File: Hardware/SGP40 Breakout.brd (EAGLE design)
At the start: 25.4 x 25.4 mm, 44 parts, among them J2 QWIIC_RIGHT_ANGLE, J4 QWIIC_RIGHT_ANGLE, U1 SGP40

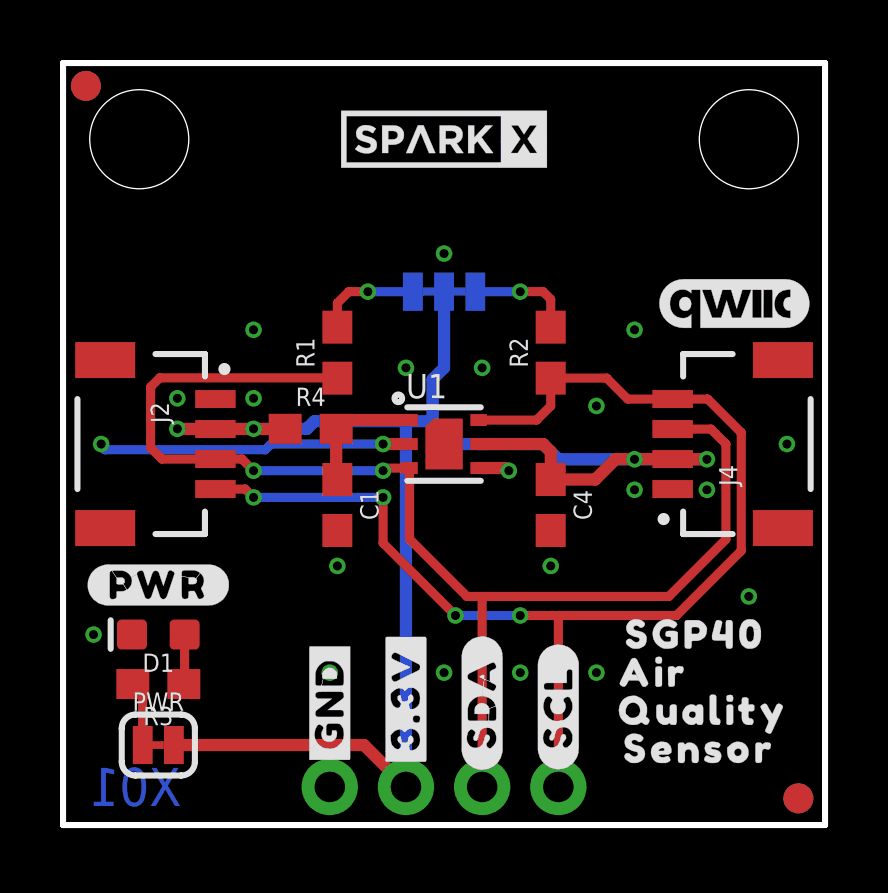
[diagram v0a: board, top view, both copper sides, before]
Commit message: Update logos on board
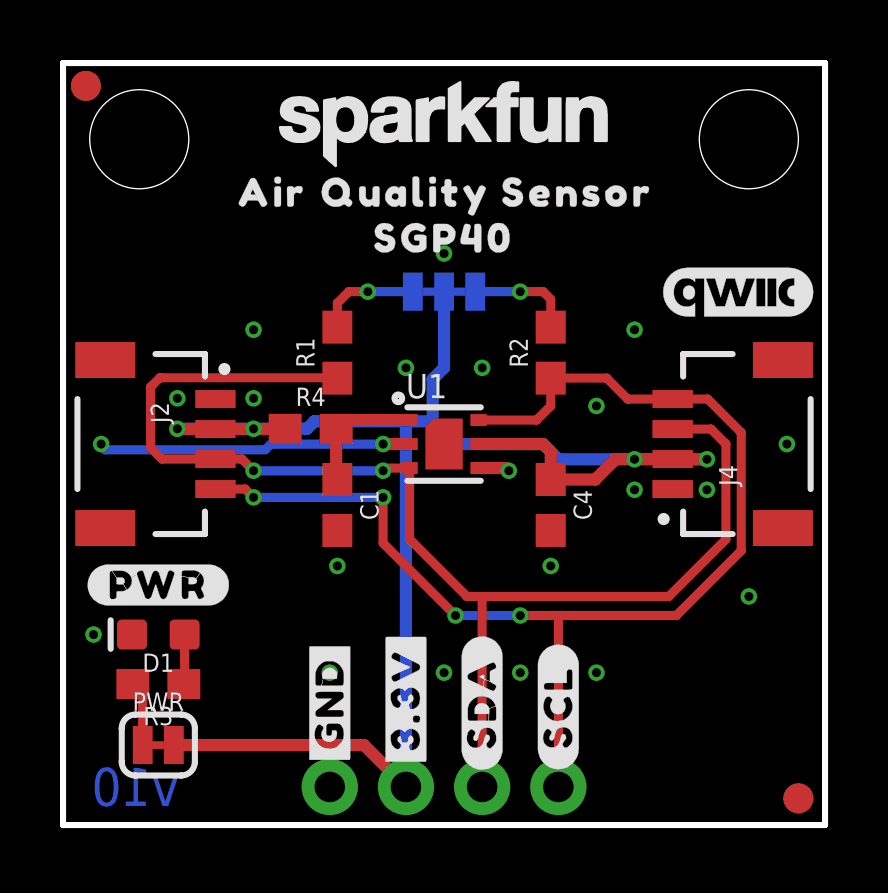
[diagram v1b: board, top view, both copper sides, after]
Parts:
- removed U$10, U$18: SPARKX-LOGO3, SparkX:SPARKX-SMALL
- removed U$16: (no value), SparkFun-Aesthetics:QWIIC_5MM
- added LOGO2: QWIIC_LOGO_5MM, SparkFun-Aesthetics:QWIIC_5MM
- added LOGO3, LOGO6: SFE_LOGO_NAME.1_INCH, SparkFun-Aesthetics:SFE_LOGO_NAME_.1
- added LOGO4: SFE_LOGO_FLAME.1_INCH, SparkFun-Aesthetics:SFE_LOGO_FLAME_.1
- moved U$23 20.4 mm to (6.99, 21.1)
- moved U$25 19.9 mm to (11.4, 21.1)
- moved U$29 19.0 mm to (17.1, 21.1)
- moved U$19 15.6 mm to (12.7, 19.6)
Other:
- board text added: "Revised by: Priyanka Makin"
- board text added: "v10"
- board text removed: "X01"
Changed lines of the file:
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@@
 <?xml version="1.0" encoding="utf-8"?>
 <!DOCTYPE eagle SYSTEM "eagle.dtd">
-<eagle version="9.6.2">
+<eagle version="9.5.2">
 <drawing>
 <settings>
@@
 <layer number="23" name="tOrigins" color="15" fill="1" visible="yes" active="yes"/>
 <layer number="24" name="bOrigins" color="15" fill="1" visible="yes" active="yes"/>
-<layer number="25" name="tNames" color="7" fill="1" visible="yes" active="yes"/>
-<layer number="26" name="bNames" color="7" fill="1" visible="yes" active="yes"/>
-<layer number="27" name="tValues" color="7" fill="1" visible="yes" active="yes"/>
-<layer number="28" name="bValues" color="7" fill="1" visible="yes" active="yes"/>
-<layer number="29" name="tStop" color="7" fill="3" visible="yes" active="yes"/>
-<layer number="30" name="bStop" color="7" fill="6" visible="yes" active="yes"/>
-<layer number="31" name="tCream" color="7" fill="4" visible="yes" active="yes"/>
-<layer number="32" name="bCream" color="7" fill="5" visible="yes" active="yes"/>
-<layer number="33" name="tFinish" color="6" fill="3" visible="yes" active="yes"/>
-<layer number="34" name="bFinish" color="6" fill="6" visible="yes" active="yes"/>
-<layer number="35" name="tGlue" color="7" fill="4" visible="yes" active="yes"/>
-<layer number="36" name="bGlue" color="7" fill="5" visible="yes" active="yes"/>
-<layer number="37" name="tTest" color="7" fill="1" visible="yes" active="yes"/>
-<layer number="38" name="bTest" color="7" fill="1" visible="yes" active="yes"/>
-<layer number="39" name="tKeepout" color="4" fill="11" visible="yes" active="yes"/>
-<layer number="40" name="bKeepout" color="1" fill="11" visible="yes" active="yes"/>
-<layer number="41" name="tRestrict" color="4" fill="10" visible="yes" active="yes"/>
-<layer number="42" name="bRestrict" color="1" fill="10" visible="yes" active="yes"/>
-<layer number="43" name="vRestrict" color="2" fill="10" visible="yes" active="yes"/>
-<layer number="44" name="Drills" color="7" fill="1" visible="yes" active="yes"/>
+<layer number="25" name="tNames" color="7" fill="1" visible="no" active="yes"/>
+<layer number="26" name="bNames" color="7" fill="1" visible="no" active="yes"/>
+<layer number="27" name="tValues" color="7" fill="1" visible="no" active="yes"/>
+<layer number="28" name="bValues" color="7" fill="1" visible="no" active="yes"/>
+<layer number="29" name="tStop" color="7" fill="3" visible="no" active="yes"/>
+<layer number="30" name="bStop" color="7" fill="6" visible="no" active="yes"/>
+<layer number="31" name="tCream" color="7" fill="4" visible="no" active="yes"/>
+<layer number="32" name="bCream" color="7" fill="5" visible="no" active="yes"/>
+<layer number="33" name="tFinish" color="6" fill="3" visible="no" active="yes"/>
+<layer number="34" name="bFinish" color="6" fill="6" visible="no" active="yes"/>
+<layer number="35" name="tGlue" color="7" fill="4" visible="no" active="yes"/>
+<layer number="36" name="bGlue" color="7" fill="5" visible="no" active="yes"/>
+<layer number="37" name="tTest" color="7" fill="1" visible="no" active="yes"/>
+<layer number="38" name="bTest" color="7" fill="1" visible="no" active="yes"/>
+<layer number="39" name="tKeepout" color="4" fill="11" visible="no" active="yes"/>
+<layer number="40" name="bKeepout" color="1" fill="11" visible="no" active="yes"/>
+<layer number="41" name="tRestrict" color="4" fill="10" visible="no" active="yes"/>
+<layer number="42" name="bRestrict" color="1" fill="10" visible="no" active="yes"/>
+<layer number="43" name="vRestrict" color="2" fill="10" visible="no" active="yes"/>
+<layer number="44" name="Drills" color="7" fill="1" visible="no" active="yes"/>
 <layer number="45" name="Holes" color="7" fill="1" visible="yes" active="yes"/>
-<layer number="46" name="Milling" color="3" fill="1" visible="yes" active="yes"/>
-<layer number="47" name="Measures" color="7" fill="1" visible="yes" active="yes"/>
-<layer number="48" name="Document" color="7" fill="1" visible="yes" active="yes"/>
-<layer number="49" name="Reference" color="7" fill="1" visible="yes" active="yes"/>
-<layer number="50" name="dxf" color="7" fill="1" visible="yes" active="yes"/>
+<layer number="46" name="Milling" color="3" fill="1" visible="no" active="yes"/>
+<layer number="47" name="Measures" color="7" fill="1" visible="no" active="yes"/>
+<layer number="48" name="Document" color="7" fill="1" visible="no" active="yes"/>
+<layer number="49" name="Reference" color="7" fill="1" visible="no" active="yes"/>
+<layer number="50" name="dxf" color="7" fill="1" visible="no" active="yes"/>
 <layer number="51" name="tDocu" color="6" fill="1" visible="yes" active="yes"/>
-<layer number="52" name="bDocu" color="7" fill="1" visible="yes" active="yes"/>
+<layer number="52" name="bDocu" color="7" fill="1" visible="no" active="yes"/>
 <layer number="91" name="Nets" color="2" fill="1" visible="no" active="no"/>
 <layer number="92" name="Busses" color="1" fill="1" visible="no" active="no"/>
@@
 <wire x1="25.4" y1="25.4" x2="25.4" y2="0" width="0.2032" layer="20"/>
 <wire x1="25.4" y1="0" x2="0" y2="0" width="0.2032" layer="20"/>
-<text x="2.413" y="1.27" size="1.27" layer="16" font="vector" ratio="15" rot="MR0" align="center">X01</text>
+<text x="2.413" y="1.27" size="1.27" layer="16" font="vector" ratio="15" rot="MR0" align="center">v10</text>
 <dimension x1="0" y1="0" x2="0" y2="25.4" x3="-5.08" y3="12.7" textsize="1.778" textratio="15" layer="47" unit="inch"/>
 <dimension x1="2.54" y1="22.86" x2="2.54" y2="0" x3="-1.27" y3="11.43" textsize="1.778" textratio="15" layer="47" unit="inch"/>
@@
 1.6mm Thickness
 HASL Finish</text>
+<text x="57.15" y="-12.7" size="1.778" layer="51" font="vector" ratio="10">Revised by: Priyanka Makin</text>
 </plain>
 <attributes>
@@
 </element>
 <element name="U$15" library="SparkFun-Buzzard" package="I2C" value="" x="14.605" y="15.875" smashed="yes" rot="MR0"/>
-<element name="U$16" library="SparkFun-Aesthetics" package="QWIIC_5MM" value="" x="22.352" y="17.399" smashed="yes"/>
 <element name="U1" library="SparkFun-Sensors" package="SGP40" value="SGP40" x="12.7" y="12.7" smashed="yes">
 <attribute name="DIGIKEY_PART" value="1649-SGP40-D-R4CT-ND" x="12.7" y="12.7" size="1.778" layer="27" ratio="15" display="off"/>
@@
 <attribute name="VALUE" value="4.7" x="8.255" y="12.446" size="0.6096" layer="27" font="vector" ratio="20" align="top-center"/>
 </element>
-<element name="U$10" library="SparkX" package="SPARKX-SMALL" value="SPARKX-LOGO3" x="12.7" y="22.86" smashed="yes"/>
-<element name="U$18" library="SparkX" package="SPARKX-SMALL" value="SPARKX-LOGO3" x="12.7" y="22.86" smashed="yes" rot="MR0"/>
 <element name="LOGO1" library="SparkFun-Aesthetics" package="ORDERING_INSTRUCTIONS" value="SPECIAL_INSTRUCTIONS-ORDERING" x="30.48" y="50.8" smashed="yes"/>
-<element name="U$19" library="output" package="SGP400" value="" x="21.082" y="6.35" smashed="yes"/>
+<element name="U$19" library="output" package="SGP400" value="" x="12.7" y="19.558" smashed="yes"/>
 <element name="U$20" library="output" package="SGP400" value="" x="21.844" y="6.35" smashed="yes" rot="MR0"/>
-<element name="U$23" library="output" package="AIR0" value="" x="19.685" y="5.08" smashed="yes"/>
+<element name="U$23" library="output" package="AIR0" value="" x="6.985" y="21.082" smashed="yes"/>
 <element name="U$24" library="output" package="AIR0" value="" x="23.114" y="5.08" smashed="yes" rot="MR0"/>
-<element name="U$25" library="output" package="QUALITY0" value="" x="21.336" y="3.81" smashed="yes"/>
+<element name="U$25" library="output" package="QUALITY0" value="" x="11.43" y="21.082" smashed="yes"/>
 <element name="U$28" library="output" package="QUALITY0" value="" x="21.463" y="3.81" smashed="yes" rot="MR0"/>
-<element name="U$29" library="output" package="SENSOR0" value="" x="21.209" y="2.54" smashed="yes"/>
+<element name="U$29" library="output" package="SENSOR0" value="" x="17.145" y="21.082" smashed="yes"/>
 <element name="U$30" library="output" package="SENSOR0" value="" x="21.717" y="2.54" smashed="yes" rot="MR0"/>
 <element name="U$31" library="output" package="ADR#_0X590" value="" x="12.7" y="10.16" smashed="yes" rot="MR0"/>
@@
 <element name="U$3" library="output" package="#SDA#0" value="" x="13.97" y="4.064" smashed="yes" rot="MR90"/>
 <element name="U$4" library="output" package="#SCL#0" value="" x="16.51" y="3.937" smashed="yes" rot="MR90"/>
+<element name="LOGO2" library="SparkFun-Aesthetics" package="QWIIC_5MM" value="QWIIC_LOGO_5MM" x="22.479" y="17.78" smashed="yes"/>
+<element name="LOGO3" library="SparkFun-Aesthetics" package="SFE_LOGO_NAME_.1" value="SFE_LOGO_NAME.1_INCH" x="12.7" y="20.32" smashed="yes" rot="MR0"/>
+<element name="LOGO4" library="SparkFun-Aesthetics" package="SFE_LOGO_FLAME_.1" value="SFE_LOGO_FLAME.1_INCH" x="10.922" y="22.86" smashed="yes" rot="MR0"/>
+<element name="LOGO6" library="SparkFun-Aesthetics" package="SFE_LOGO_NAME_.1" value="SFE_LOGO_NAME.1_INCH" x="12.7" y="23.368" smashed="yes"/>
 </elements>
 <signals>

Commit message: Petes updates:
Update version number in sch
Added 2 more standoffs (moved power LED and jumper)
Update value of qwiic connector in schematic
Update legacy vector font
Add qwiic connector and header measure
Switched I2C pullup resistors to 4.7k
Add min/max voltage of IC to sch
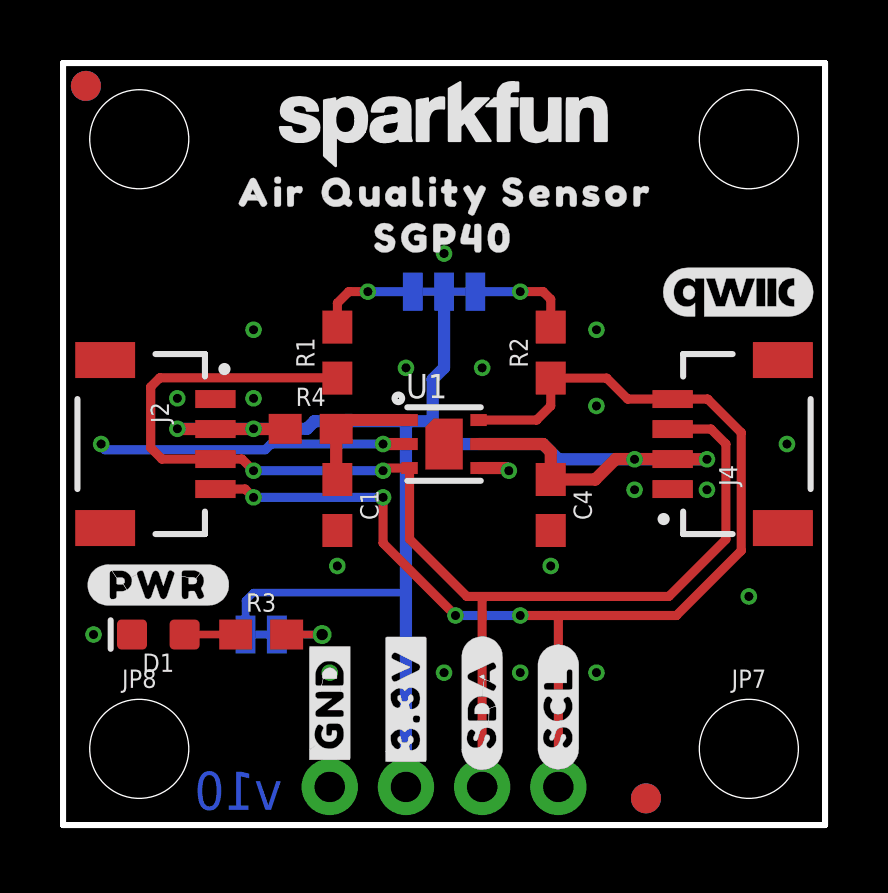
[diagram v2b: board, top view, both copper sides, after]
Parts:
- added JP7, JP8: STAND-OFF, SparkFun-Hardware:STAND-OFF
- J2, J4: value QWIIC_RIGHT_ANGLE -> QWIIC_RA
- R1, R2: value 10k -> 4.7k
- moved U$20 12.7 mm to (21.8, 19.1)
- moved U$24 12.7 mm to (23.1, 17.8)
- moved U$28 12.7 mm to (21.5, 16.5)
- moved U$30 12.7 mm to (21.7, 15.2)
- moved JP2 5.08 mm to (19.4, 0.89)
- moved JP5 5.08 mm to (19.4, 0.89)
- moved PWR 5.03 mm to (6.60, 6.35), flipped to the bottom
- moved LOGO5 3.81 mm to (2.54, 7.62)
- moved R3 3.81 mm to (6.60, 6.35), turned to 0 degrees
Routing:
- net 3.3V: track 55.8 -> 54.1 mm
- net N$1: track 2.17 -> 2.69 mm, vias 0 -> 1

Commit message: Update silk
LED label plain text
Inverted bubbled for LED jumper
Make SDA/SCL pin labels square on one side
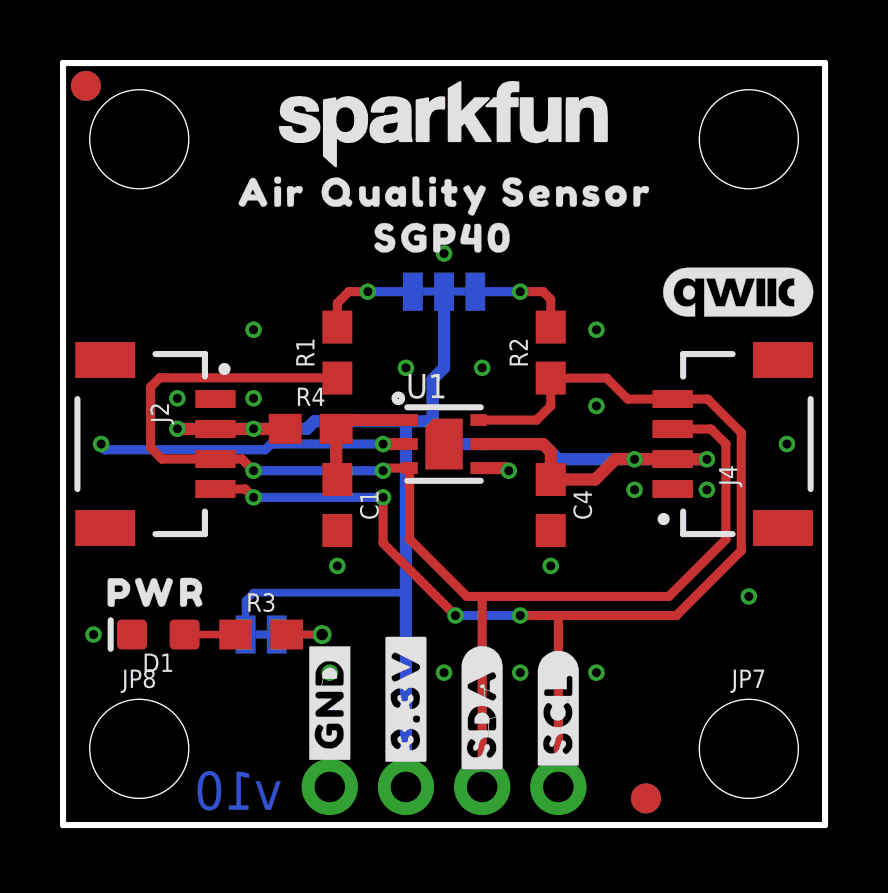
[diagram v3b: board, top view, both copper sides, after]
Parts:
- removed U$32: (no value), output:#PWR#0
- added U$5: (no value), output:PWR0
- added U$6: (no value), output:#PWR#0
- moved LOGO5 20.9 mm to (22.9, 12.7)
- moved U$3 2.54 mm to (14.0, 1.52)
- moved U$35 2.54 mm to (14.0, 1.52)
- moved U$36 2.29 mm to (16.5, 1.65)
- moved U$4 2.29 mm to (16.5, 1.65)
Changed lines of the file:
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@@
 <?xml version="1.0" encoding="utf-8"?>
 <!DOCTYPE eagle SYSTEM "eagle.dtd">
-<eagle version="9.5.2">
+<eagle version="9.6.2">
 <drawing>
 <settings>
@@
 <attribute name="NAME" x="6.604" y="7.493" size="0.6096" layer="26" font="vector" ratio="20" rot="MR0" align="bottom-center"/>
 </element>
-<element name="LOGO5" library="SparkFun-Aesthetics" package="OSHW-LOGO-S" value="OSHW-LOGOS" x="2.54" y="7.62" smashed="yes" rot="MR0"/>
+<element name="LOGO5" library="SparkFun-Aesthetics" package="OSHW-LOGO-S" value="OSHW-LOGOS" x="22.86" y="12.7" smashed="yes" rot="MR0"/>
 <element name="J1" library="SparkFun-Connectors" package="1X04_NO_SILK" value="" x="8.89" y="1.27" smashed="yes" rot="MR180">
 <attribute name="NAME" x="7.62" y="-0.127" size="0.6096" layer="26" font="vector" ratio="20" rot="MR180"/>
@@
 <element name="U$30" library="output" package="SENSOR0" value="" x="21.717" y="15.24" smashed="yes" rot="MR0"/>
 <element name="U$31" library="output" package="ADR#_0X590" value="" x="12.7" y="10.16" smashed="yes" rot="MR0"/>
-<element name="U$32" library="output" package="#PWR#0" value="" x="3.175" y="8.001" smashed="yes"/>
 <element name="U$33" library="output" package="#GND#0" value="" x="8.89" y="4.064" smashed="yes" rot="R90"/>
 <element name="U$34" library="output" package="#3#3V#0" value="" x="11.43" y="4.191" smashed="yes" rot="R90"/>
-<element name="U$35" library="output" package="#SDA#0" value="" x="13.97" y="4.064" smashed="yes" rot="R90"/>
-<element name="U$36" library="output" package="#SCL#0" value="" x="16.51" y="3.937" smashed="yes" rot="R90"/>
+<element name="U$35" library="output" package="#SDA#0" value="" x="13.97" y="1.524" smashed="yes" rot="R90"/>
+<element name="U$36" library="output" package="#SCL#0" value="" x="16.51" y="1.651" smashed="yes" rot="R90"/>
 <element name="U$1" library="output" package="#GND#0" value="" x="8.89" y="4.064" smashed="yes" rot="MR90"/>
 <element name="U$2" library="output" package="#3#3V#0" value="" x="11.43" y="4.191" smashed="yes" rot="MR90"/>
-<element name="U$3" library="output" package="#SDA#0" value="" x="13.97" y="4.064" smashed="yes" rot="MR90"/>
-<element name="U$4" library="output" package="#SCL#0" value="" x="16.51" y="3.937" smashed="yes" rot="MR90"/>
+<element name="U$3" library="output" package="#SDA#0" value="" x="13.97" y="1.524" smashed="yes" rot="MR90"/>
+<element name="U$4" library="output" package="#SCL#0" value="" x="16.51" y="1.651" smashed="yes" rot="MR90"/>
 <element name="LOGO2" library="SparkFun-Aesthetics" package="QWIIC_5MM" value="QWIIC_LOGO_5MM" x="22.479" y="17.78" smashed="yes"/>
 <element name="LOGO3" library="SparkFun-Aesthetics" package="SFE_LOGO_NAME_.1" value="SFE_LOGO_NAME.1_INCH" x="12.7" y="20.32" smashed="yes" rot="MR0"/>
@@
 <attribute name="VALUE" x="2.54" y="0.508" size="0.6096" layer="27" font="vector" ratio="20" align="top-center"/>
 </element>
+<element name="U$5" library="output" package="PWR0" value="" x="0.762" y="7.747" smashed="yes"/>
+<element name="U$6" library="output" package="#PWR#0" value="" x="5.715" y="6.35" smashed="yes" rot="MR0"/>
 </elements>
 <signals>

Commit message: Design review updates
SDA, SCL buzzard placement
3.3V trace → 20
Add operating current to sch
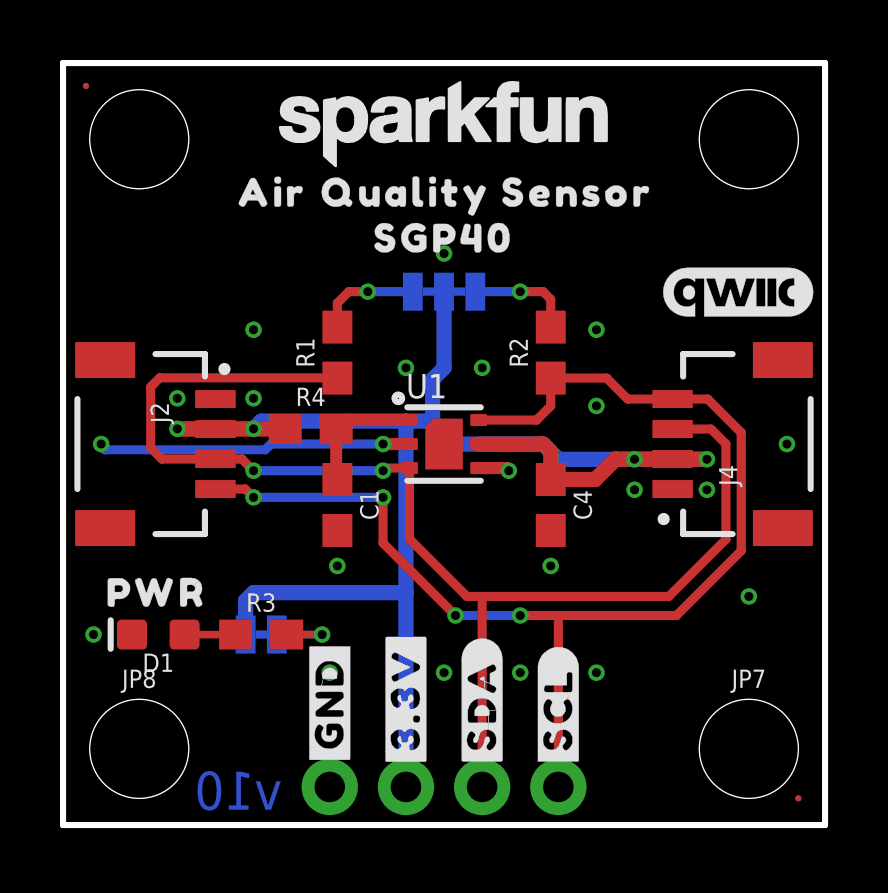
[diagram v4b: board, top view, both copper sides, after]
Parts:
- JP1, JP2, JP5, JP6: value FIDUCIAL1X2 -> FIDUCIAL0.2MM; device SparkFun-Aesthetics:FIDUCIAL-1X2 -> SparkFun-Aesthetics:FIDUCIAL-0.2MM
- moved JP2 5.08 mm to (24.5, 0.89)
- moved JP5 5.08 mm to (24.5, 0.89)
- moved U$3 0.25 mm to (14.0, 1.78)
- moved U$35 0.25 mm to (14.0, 1.78)
- moved U$36 0.13 mm to (16.5, 1.78)
- moved U$4 0.13 mm to (16.5, 1.78)
